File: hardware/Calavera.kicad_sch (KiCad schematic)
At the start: 25 parts, among them Q1 Q_DUAL_NMOS, U1 AT42QT1012, U2 LMV932

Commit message: v0.3.0 see changelog for details
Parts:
- removed Q1: Q_DUAL_NMOS, Calavera:SOT-363_NX138BKS_Handsolder, symbol Calavera:Q_DUAL_NMOS
- added Q1: DMN65D8L, Calavera:SOT-23_NMOS_DMN65D8L, symbol Calavera:Q_NMOS_GDS
- added SW1: SW_SPDT, Calavera:Slider_Switch_C&K_AYZ0102AGRLC_SPDT_RightAngle, symbol Calavera:SW_SPDT
- BT1: footprint Calavera:CR2032_Multicomp_MP000357_Alternative -> Calavera:CR2032_Keystone_3024; Comments (none) -> Alternative part 3034TR is tape and reel, but it's also sol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; Digikey PN (none) -> 36-3034-ND; Farnell PN (none) -> 2959382; MPN MP000357 -> 3034; Manufacturer  Multicomp -> Keystone
- U1: Digikey PN (none) -> 401-2012-1-ND
- U2: Digikey PN (none) -> LMV932DR2GOSCT-ND
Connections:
- net VLEDK2 is gone; now on net VLEDK: D2.1 (K)
- net Cap_Out: now also Q1.1 (G)
- net GND: now also Q1.3 (S)
- net VCC: now also SW1.2 (B); no longer BT1.+
- net VLEDK1 renamed VLEDK
- net VLEDK: now also Q1.2 (D)
- new net: BT1.+, SW1.3 (C)
- no-connect marks 0 -> 1
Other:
- note removed: "A lithium coin cell starts at 3V and will drop to around 2.5V"
- moved on the sheet: BT1, D1, D2, R5, R6

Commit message: Added KiBot as CICD and removed CircleCI Fixed some DRC/ERC errors and tweaked the files so KiBot accepts them and generates artifacts from them
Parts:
- G1: footprint Calavera:Calavera_Cap_Pad -> Calavera:Cap_Pad
- R5, R6: value R_Small_US -> RΩ
- U1: footprint Calavera:SOT23-6-AT42QT1012_Handsolder -> Calavera:SOT23-6-AT42QT1012; MPN AT42QT1012-TSHR -> AT42QT1012-TSHR
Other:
- note added: "Current limiting resistor values depend on the LED used"
- title: (none) -> Calavera Badge
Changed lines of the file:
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@@
 (kicad_sch (version 20211123) (generator eeschema)
   (paper "A4")
+  (title_block
+    (title "Calavera Badge")
+    (date "${TODAY}")
+    (rev "v0.3.0")
+    (comment 1 "Files generated from commit ${GIT_HASH}")
+  )
   (junction (at 187.96 31.75) (diameter 0) (color 0 0 0 0)
   )
@@
   (text "Misc" (at 264.16 143.51 0)
     (effects (font (size 1.27 1.27) (thickness 0.254) bold) (justify left bottom))
+  )
+  (text "Current limiting resistor values\ndepend on the LED used"
+    (at 151.13 112.395 90)
+    (effects (font (size 1.27 1.27)) (justify left bottom))
   )
   (text "Jumper" (at 21.59 81.28 0)
@@
     (property "Reference" "U1" (id 0) (at 74.93 55.88 0))
     (property "Value" "AT42QT1012" (id 1) (at 78.74 58.42 0))
-    (property "Footprint" "Calavera:SOT23-6-AT42QT1012_Handsolder" (id 2) (at 71.12 48.26 0)
+    (property "Footprint" "Calavera:SOT23-6-AT42QT1012" (id 2) (at 71.12 48.26 0)
       (effects (font (size 1.27 1.27)) hide)
     )
@@
       (effects (font (size 1.27 1.27)) hide)
     )
-    (property "MPN" "AT42QT1012-TSHR " (id 4) (at 71.12 48.26 0)
+    (property "MPN" "AT42QT1012-TSHR" (id 4) (at 71.12 48.26 0)
       (effects (font (size 1.27 1.27)) hide)
     )
@@
       (effects (font (size 1.524 1.524)) hide)
     )
-    (property "Footprint" "Calavera:Calavera_Cap_Pad" (id 2) (at 34.29 45.72 0)
+    (property "Footprint" "Calavera:Cap_Pad" (id 2) (at 34.29 45.72 0)
       (effects (font (size 1.27 1.27)) hide)
     )
@@
       (effects (font (size 1.27 1.27)) (justify left))
     )
-    (property "Value" "R_Small_US" (id 1) (at 156.6672 92.583 0)
+    (property "Value" "RΩ" (id 1) (at 156.6672 92.583 0)
       (effects (font (size 1.27 1.27)) (justify left))
     )
@@
       (effects (font (size 1.27 1.27)) (justify left))
     )
-    (property "Value" "R_Small_US" (id 1) (at 173.1772 92.583 0)
+    (property "Value" "RΩ" (id 1) (at 173.1772 92.583 0)
       (effects (font (size 1.27 1.27)) (justify left))
     )
@@
       (effects (font (size 1.27 1.27)) hide)
     )
-    (property "Datasheet" "https://www.diodes.com/assets/Datasheets/DMN65D8L.pdf" (id 3) (at 76.2 99.06 0)
+    (property "Datasheet" "~" (id 3) (at 76.2 99.06 0)
       (effects (font (size 1.27 1.27)) hide)
     )
@@
       (effects (font (size 1.27 1.27)) hide)
     )
-    (property "Datasheet" "https://www.ckswitches.com/media/1431/ayz.pdf" (id 3) (at 243.84 96.52 0)
+    (property "Datasheet" "~" (id 3) (at 243.84 96.52 0)
       (effects (font (size 1.27 1.27)) hide)
     )
@@
     )
     (path "/00000000-0000-0000-0000-00005d3703e7"
-      (reference "G1") (unit 1) (value "HeartPad") (footprint "Calavera:Calavera_Cap_Pad")
+      (reference "G1") (unit 1) (value "HeartPad") (footprint "Calavera:Cap_Pad")
     )
     (path "/00000000-0000-0000-0000-00005d5d7396"
@@
     )
     (path "/00000000-0000-0000-0000-00005d409c2b"
-      (reference "R5") (unit 1) (value "R_Small_US") (footprint "Calavera:0805-R_Handsolder")
+      (reference "R5") (unit 1) (value "RΩ") (footprint "Calavera:0805-R_Handsolder")
     )
     (path "/00000000-0000-0000-0000-00005d40a0ac"
-      (reference "R6") (unit 1) (value "R_Small_US") (footprint "Calavera:0805-R_Handsolder")
+      (reference "R6") (unit 1) (value "RΩ") (footprint "Calavera:0805-R_Handsolder")
     )
     (path "/00000000-0000-0000-0000-00005d45762a"
@@
     )
     (path "/00000000-0000-0000-0000-00005d36f6bf"
-      (reference "U1") (unit 1) (value "AT42QT1012") (footprint "Calavera:SOT23-6-AT42QT1012_Handsolder")
+      (reference "U1") (unit 1) (value "AT42QT1012") (footprint "Calavera:SOT23-6-AT42QT1012")
     )
     (path "/00000000-0000-0000-0000-00005d4485a3"

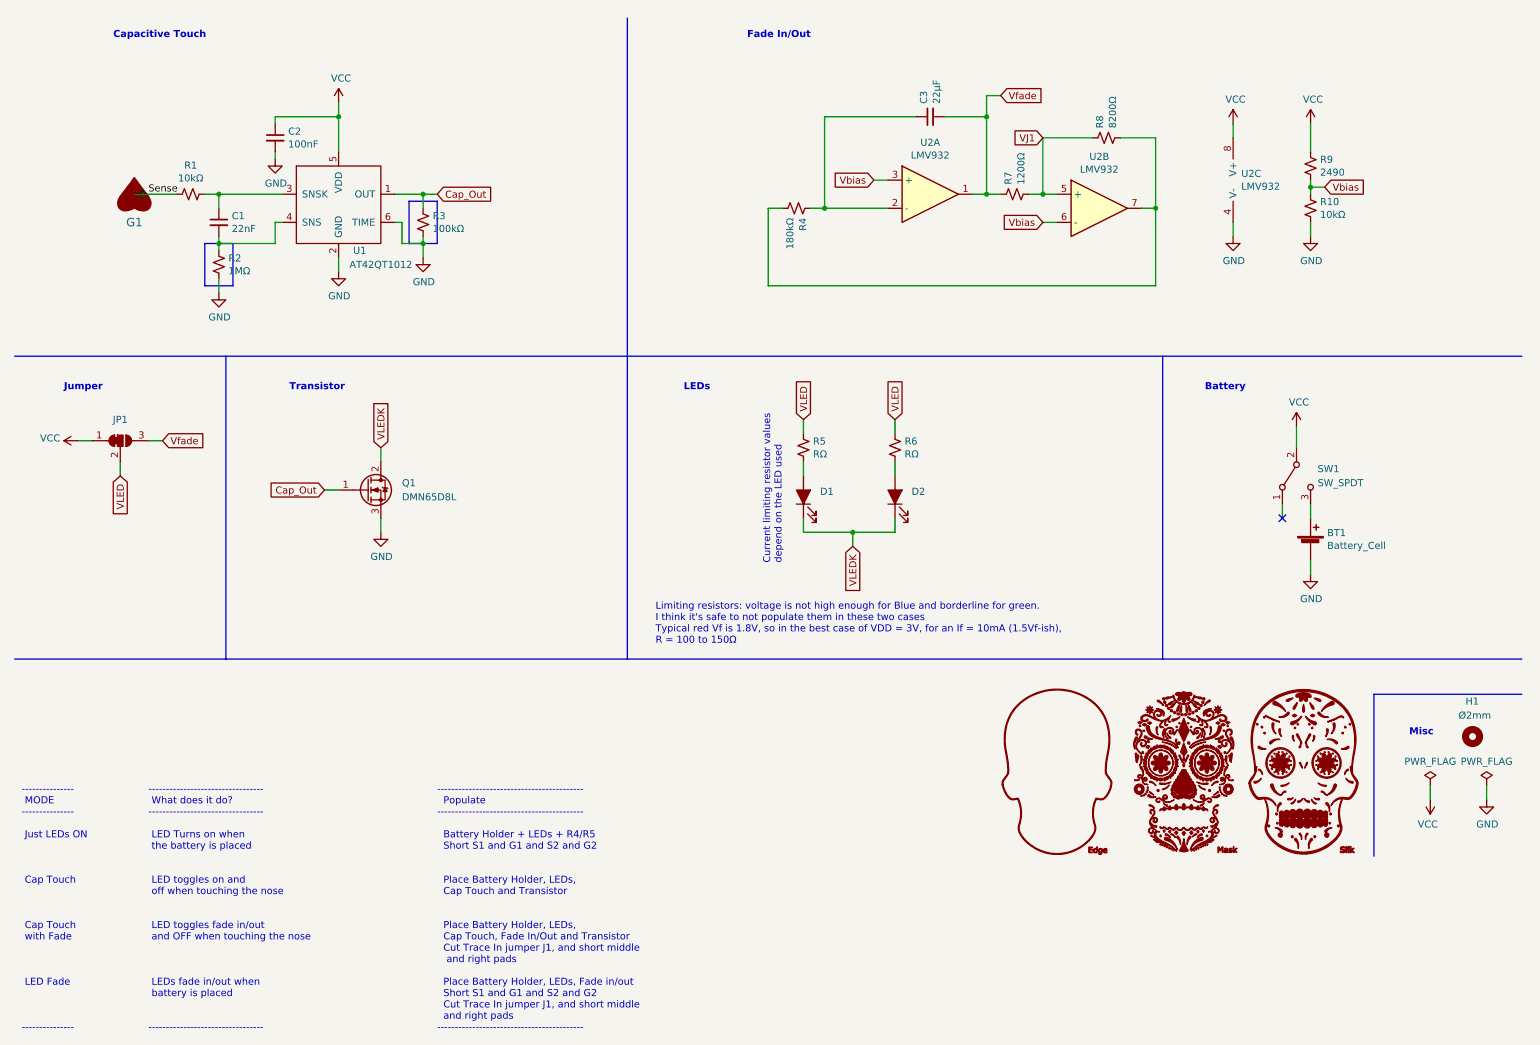
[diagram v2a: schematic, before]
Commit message: Small edit of the Art. Small changes here and there to account for new DRCs in KiCad 7
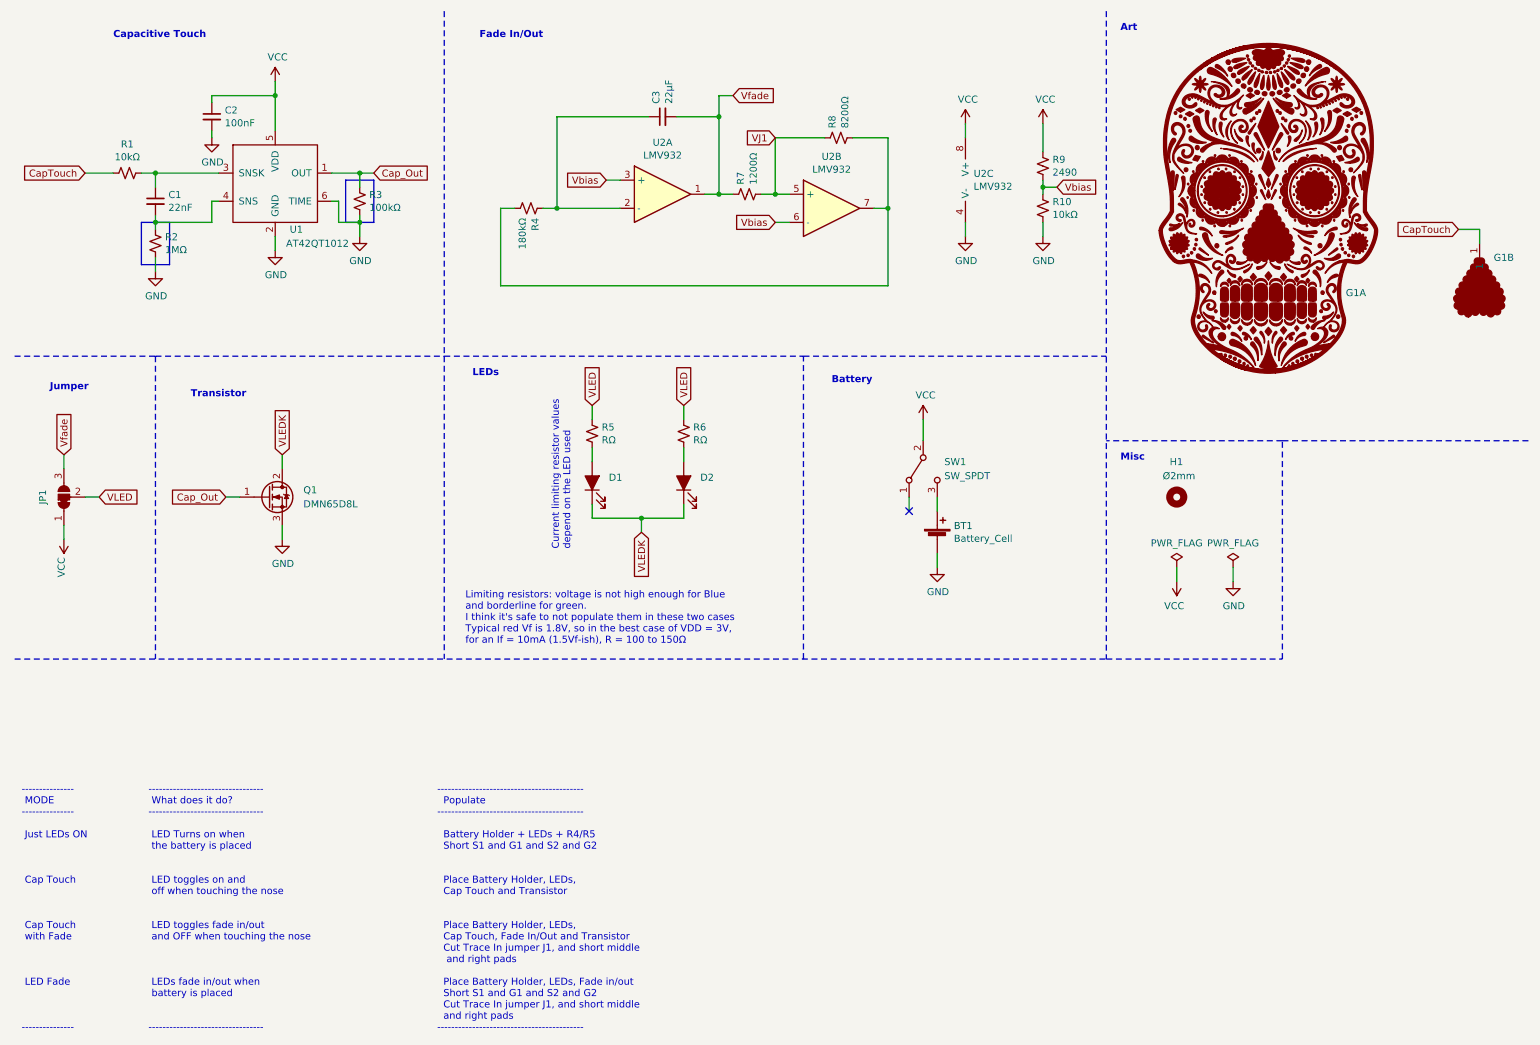
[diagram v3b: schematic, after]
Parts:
- removed G1: HeartPad, Calavera:Cap_Pad, symbol Calavera:HeartPad
- removed G2: Edge, Calavera:Calavera_Board_Margins, symbol Calavera:Edge
- removed G3: Mask, Calavera:Calavera_SolderMask_1200dpi_Border, symbol Calavera:Mask
- removed G4: Silk, Calavera:Calavera_SilkScreen_1200dpi, symbol Calavera:Silk
- added G1: Calavera_Art, Calavera:Calavera_Art, symbol Calavera:Calavera_Art
- D1, D2: symbol Calavera:LED_ALT-Device -> Calavera:LED_3mm_TH
- H1: footprint Calavera:MountingHole_2mm -> Calavera:MountingHole_1.75mm
- U2: symbol Calavera:Opamp_Dual_Generic-Device -> Calavera:Opamp_Dual
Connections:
- net Sense renamed CapTouch
- net CapTouch: now also G1.1
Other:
- note added: "Art"
- moved on the sheet: BT1, C1, C2, C3, D1, D2, H1, JP1, Q1, R1, R10, R2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

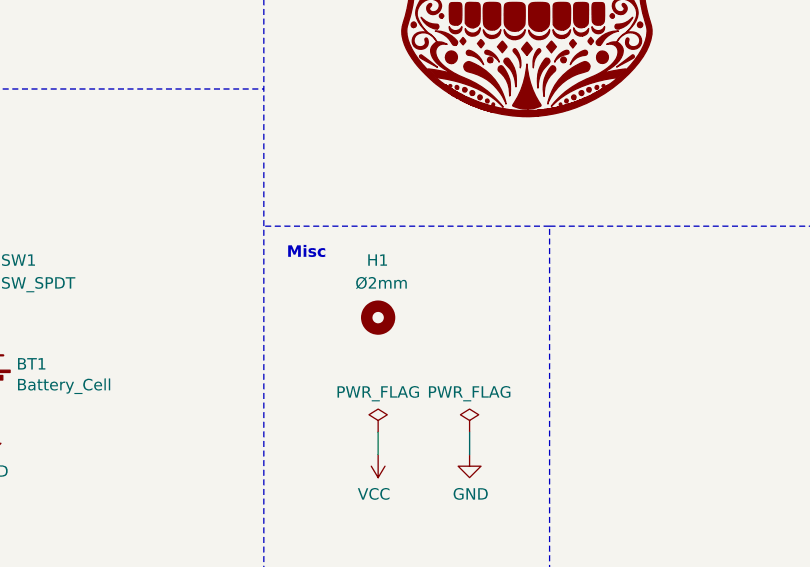
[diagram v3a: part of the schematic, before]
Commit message: Hand tweaks to the art to avoid most of the ERC errors
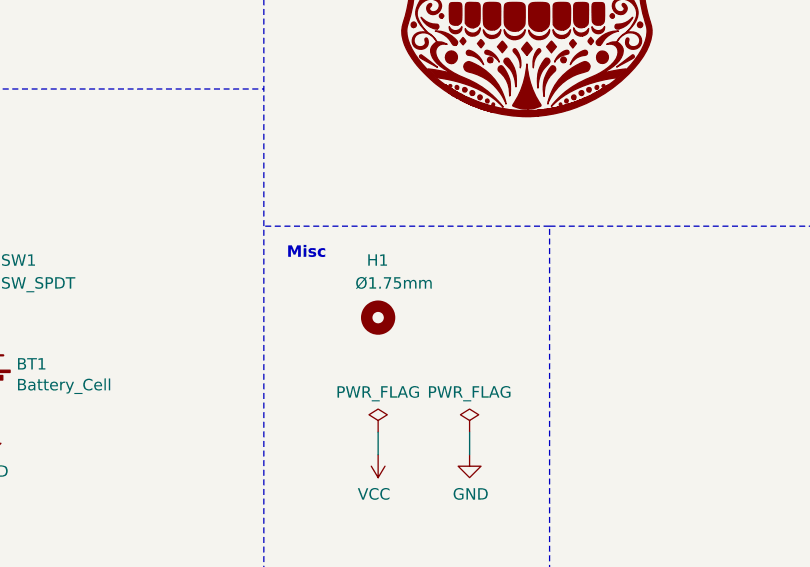
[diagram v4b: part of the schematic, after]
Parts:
- H1: value Ø2mm -> Ø1.75mm
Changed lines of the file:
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@@
       (effects (font (size 1.27 1.27)) (justify left))
     )
-    (property "Value" "Ø2mm" (at 219.71 96.52 0)
+    (property "Value" "Ø1.75mm" (at 219.71 96.52 0)
       (effects (font (size 1.27 1.27)) (justify left))
     )

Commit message: Tweaks on the project for KiBot
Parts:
- H1, JP1: now left out of the parts list
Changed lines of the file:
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@@
+      (effects (font (size 1.27 1.27)) hide)
+    )
+    (property "Tolerance" "" (at 33.02 41.91 0)
       (effects (font (size 1.27 1.27)) hide)
     )
@@
       (effects (font (size 1.27 1.27)) hide)
     )
+    (property "Tolerance" "" (at 38.1 46.99 0)
+      (effects (font (size 1.27 1.27)) hide)
+    )
     (pin "1")
     (pin "2")
@@
       (effects (font (size 1.27 1.27)) hide)
     )
+    (property "Tolerance" "" (at 38.1 54.61 0)
+      (effects (font (size 1.27 1.27)) hide)
+    )
     (pin "1")
     (pin "2")
@@
     )
     (property "Digikey PN" "401-2012-1-ND" (at 59.69 44.45 0)
+      (effects (font (size 1.27 1.27)) hide)
+    )
+    (property "Tolerance" "" (at 59.69 44.45 0)
       (effects (font (size 1.27 1.27)) hide)
     )
@@
       (effects (font (size 1.27 1.27)) hide)
     )
+    (property "Tolerance" "" (at 74.93 46.99 0)
+      (effects (font (size 1.27 1.27)) hide)
+    )
     (pin "1")
     (pin "2")
@@
     )
     (property "Datasheet" "~" (at 48.26 31.75 0)
+      (effects (font (size 1.27 1.27)) hide)
+    )
+    (property "Tolerance" "" (at 48.26 31.75 0)
       (effects (font (size 1.27 1.27)) hide)
     )
@@
       (effects (font (size 1.27 1.27)) hide)
     )
+    (property "Tolerance" "" (at 116.84 97.79 0)
+      (effects (font (size 1.27 1.27)) hide)
+    )
     (pin "1")
     (pin "2")
@@
       (effects (font (size 1.27 1.27)) hide)
     )
+    (property "Tolerance" "" (at 133.35 97.79 0)
+      (effects (font (size 1.27 1.27)) hide)
+    )
     (pin "1")
     (pin "2")
@@
       (effects (font (size 1.27 1.27)) hide)
     )
+    (property "Tolerance" "" (at 116.84 88.9 0)
+      (effects (font (size 1.27 1.27)) hide)
+    )
     (pin "1")
     (pin "2")
@@
       (effects (font (size 1.27 1.27)) hide)
     )
+    (property "Tolerance" "" (at 133.35 88.9 0)
+      (effects (font (size 1.27 1.27)) hide)
+    )
     (pin "1")
     (pin "2")
@@
     )
     (property "Farnell PN" "2959382" (at 179.07 107.95 0)
+      (effects (font (size 1.27 1.27)) hide)
+    )
+    (property "Tolerance" "" (at 179.07 107.95 0)
       (effects (font (size 1.27 1.27)) hide)
     )
@@
   )
   (symbol (lib_id "Calavera:SolderJumper_3_Bridged12-Jumper") (at 21.59 100.33 90) (unit 1)
-    (in_bom yes) (on_board yes) (dnp no)
+    (in_bom no) (on_board yes) (dnp no)
     (property "Reference" "JP1" (at 17.78 100.33 0)
       (effects (font (size 1.27 1.27)))
@@
       (effects (font (size 1.27 1.27)) hide)
     )
+    (property "Tolerance" "" (at 21.59 100.33 0)
+      (effects (font (size 1.27 1.27)) hide)
+    )
     (pin "1")
     (pin "2")
@@
     )
     (property "Digikey PN" "LMV932DR2GOSCT-ND" (at 129.54 45.72 0)
+      (effects (font (size 1.27 1.27)) hide)
+    )
+    (property "Tolerance" "" (at 129.54 45.72 0)
       (effects (font (size 1.27 1.27)) hide)
     )
@@
       (effects (font (size 1.27 1.27)) hide)
     )
+    (property "Tolerance" "" (at 160.02 48.26 0)
+      (effects (font (size 1.27 1.27)) hide)
+    )
     (pin "1")
     (pin "2")
@@
       (effects (font (size 1.27 1.27)) hide)
     )
+    (property "Tolerance" "" (at 186.69 43.18 0)
+      (effects (font (size 1.27 1.27)) hide)
+    )
     (pin "1")
     (pin "2")
@@
       (effects (font (size 1.27 1.27)) hide)
     )
+    (property "Tolerance" "" (at 129.54 31.75 0)
+      (effects (font (size 1.27 1.27)) hide)
+    )
     (pin "1")
     (pin "2")
@@
       (effects (font (size 1.27 1.27)) hide)
     )
+    (property "Tolerance" "" (at 144.78 45.72 0)
+      (effects (font (size 1.27 1.27)) hide)
+    )
     (pin "1")
     (pin "2")
@@
       (effects (font (size 1.27 1.27)) hide)
     )
+    (property "Tolerance" "" (at 161.29 35.56 0)
+      (effects (font (size 1.27 1.27)) hide)
+    )
     (pin "1")
     (pin "2")
@@
       (effects (font (size 1.27 1.27)) hide)
     )
+    (property "Tolerance" "" (at 105.41 48.26 0)
+      (effects (font (size 1.27 1.27)) hide)
+    )
     (pin "1")
     (pin "2")
@@
       (effects (font (size 1.27 1.27)) hide)
     )
+    (property "Tolerance" "" (at 198.12 40.64 0)
+      (effects (font (size 1.27 1.27)) hide)
+    )
     (pin "1")
     (pin "2")
@@
       (effects (font (size 1.27 1.27)) hide)
     )
+    (property "Tolerance" "" (at 198.12 48.26 0)
+      (effects (font (size 1.27 1.27)) hide)
+    )
     (pin "1")
     (pin "2")
@@
   )
   (symbol (lib_id "Mechanical:MountingHole") (at 222.25 100.33 0) (unit 1)
-    (in_bom yes) (on_board yes) (dnp no)
+    (in_bom no) (on_board yes) (dnp no)
     (property "Reference" "H1" (at 220.98 93.98 0)
       (effects (font (size 1.27 1.27)) (justify left))
@@
     )
     (property "Datasheet" "~" (at 222.25 100.33 0)
+      (effects (font (size 1.27 1.27)) hide)
+    )
+    (property "Tolerance" "" (at 222.25 100.33 0)
       (effects (font (size 1.27 1.27)) hide)
     )
@@
       (effects (font (size 1.27 1.27)) hide)
     )
-    (property "Datasheet" "~" (at 58.42 100.33 0)
+    (property "Datasheet" "https://www.diodes.com/assets/Datasheets/DMN65D8L.pdf" (at 58.42 100.33 0)
       (effects (font (size 1.27 1.27)) hide)
     )
@@
     )
     (property "Comments" "Any NMOS, really. Used a the cheapest SOT23." (at 58.42 100.33 0)
+      (effects (font (size 1.27 1.27)) hide)
+    )
+    (property "Tolerance" "" (at 58.42 100.33 0)
       (effects (font (size 1.27 1.27)) hide)
     )
@@
       (effects (font (size 1.27 1.27)) hide)
     )
+    (property "Tolerance" "" (at 176.53 95.25 0)
+      (effects (font (size 1.27 1.27)) hide)
+    )
     (pin "1")
     (pin "2")
@@
       (effects (font (size 1.27 1.27)) hide)
     )
+    (property "Tolerance" "" (at 276.86 58.42 0)
+      (effects (font (size 1.27 1.27)) hide)
+    )
     (pin "1")
     (instances
@@
       (effects (font (size 1.27 1.27)) hide)
     )
+    (property "Tolerance" "" (at 238.76 48.26 0)
+      (effects (font (size 1.27 1.27)) hide)
+    )

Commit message: Put some sense and changed resistor values to reduce the number of individual parts Removed ignored files and renamed a folder
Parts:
- added R4: 100kΩ, Calavera:0805-R_Handsolder, symbol Device:R_Small_US
- C1: Digikey PN (none) -> 732-12080-1-ND; Farnell PN (none) -> 2812566; MPN (none) -> 885342207011; Manufacturer  (none) -> Wurth; Tolerance (none) -> X7R; VRating (none) -> 250V
- C2: Digikey PN (none) -> 1276-1003-1-ND; Farnell PN (none) -> 3013476; MPN (none) -> CL21B104KBCNNNC; Manufacturer  (none) -> Samsung; Tolerance (none) -> X7R; VRating (none) -> 50V
- C3: Digikey PN (none) -> 490-GRM21BZ71A226ME15LCT-ND; Farnell PN (none) -> 4128565; MPN (none) -> GRM21BZ71A226ME15L; Manufacturer  (none) -> Murata; Tolerance (none) -> X7R; VRating (none) -> 10V
- G1, H1, JP1: Digikey PN (none) -> N/A; Farnell PN (none) -> N/A; MPN (none) -> N/A; Manufacturer  (none) -> N/A
- Q1: Farnell PN (none) -> 2543546
- R1: Comments (none) -> Any 10kΩ. Why are you buying these? You should have some so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; Digikey PN (none) -> 311-10KARCT-ND; Farnell PN (none) -> 2073612; MPN (none) -> RC0805JR-0710KL; Manufacturer  (none) -> Yageo
- R11: renamed from R10; Comments (none) -> Any 10kΩ. Why are you buying these? You should have some so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; Digikey PN (none) -> 311-10KARCT-ND; Farnell PN (none) -> 2073612; MPN (none) -> RC0805JR-0710KL; Manufacturer  (none) -> Yageo
- R5: renamed from R4; value 180kΩ -> 100kΩ
- R8: renamed from R7; value 1200Ω -> 1470Ω
- R9: renamed from R8; value 8200Ω -> 10kΩ; Comments (none) -> Any 10kΩ. Why are you buying these? You should have some so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; Digikey PN (none) -> 311-10KARCT-ND; Farnell PN (none) -> 2073612; MPN (none) -> RC0805JR-0710KL; Manufacturer  (none) -> Yageo
- SW1: Farnell PN (none) -> 2319971
- U1: Farnell PN (none) -> 1841595
- U2: Farnell PN (none) -> 2724035; MPN MV932DR2G -> LMV932DR2G
- renumbered R9 to R10, R5 to R6, R6 to R7
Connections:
- net at R9.2, U2.7: now also R4.2; no longer R5.2
- new net: R4.1, R5.2
